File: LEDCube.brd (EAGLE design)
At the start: 100.5 x 80.2 mm, 19 parts

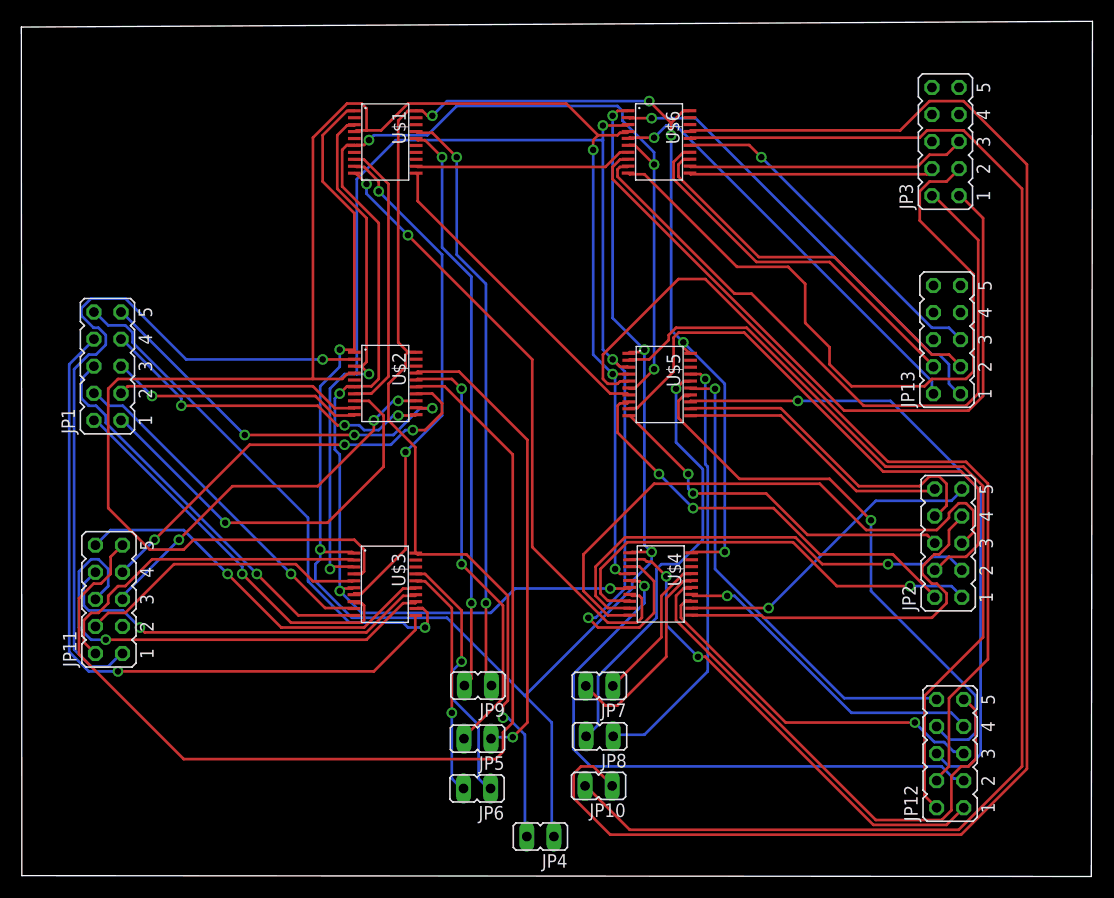
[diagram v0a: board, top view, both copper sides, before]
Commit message: Laid out MSP430 board. Not routed yet.
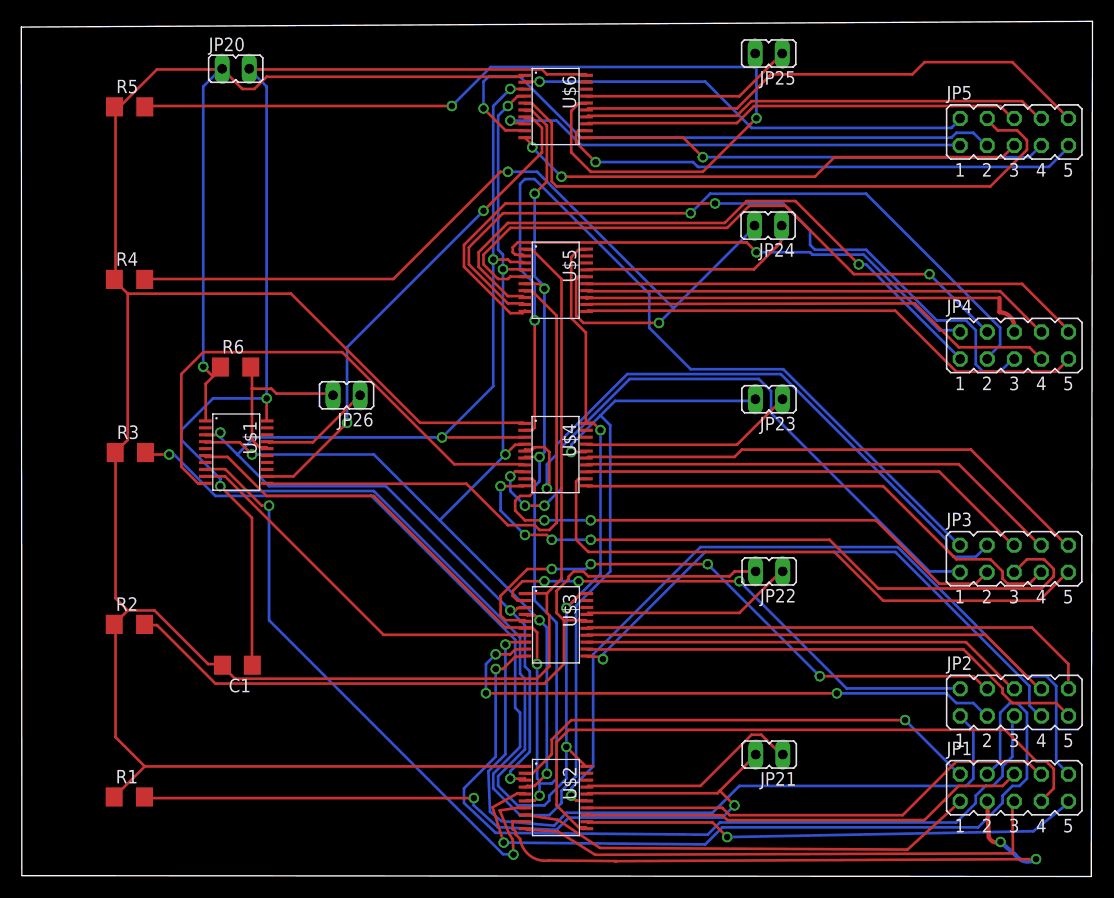
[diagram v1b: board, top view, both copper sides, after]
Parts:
- removed JP10, JP6, JP7, JP8, JP9: (no value), jumper:JP1
- removed JP11, JP12, JP13: (no value), jumper:JP5Q
- added C1: (no value), eagle-ltspice:C1206
- added JP20, JP21, JP22, JP23, JP24, JP25, JP26: (no value), jumper:JP1
- added R1, R2, R3, R4, R5, R6: (no value), rcl:R1206
- JP4, JP5: device jumper:JP1 -> jumper:JP5Q
- moved JP1 93.8 mm to (93.0, 8.52), turned to 0 degrees
- moved JP5 76.0 mm to (93.0, 70.0), turned to 0 degrees
- moved JP4 64.0 mm to (93.0, 50.0), turned to 0 degrees
- moved U$2 42.0 mm to (50.0, 7.60)
- moved JP3 39.7 mm to (93.0, 30.0), turned to 0 degrees
- moved U$1 32.3 mm to (20.0, 40.0)
- moved U$3 16.5 mm to (50.0, 23.8)
- moved JP2 16.2 mm to (93.0, 16.5), turned to 0 degrees
- moved U$4 15.6 mm to (50.0, 39.8)
- moved U$5 13.8 mm to (50.0, 56.1)
- moved U$6 10.3 mm to (50.0, 72.4)
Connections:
- net 0C0: now also JP1.2; no longer JP11.1
- net 0C1: now also JP1.4; no longer JP11.3
- net 0C2: now also JP1.6; no longer JP11.5
- net 0C3: now also JP1.8; no longer JP11.7
- net 0C4: now also JP1.10; no longer JP11.9
- net 1A0: now also JP2.1; no longer JP1.2
- net 1A1: now also JP2.3; no longer JP1.4
- net 1A2: now also JP2.5; no longer JP1.6
- net 1A3: now also JP2.7; no longer JP1.8
- net 1A4: now also JP2.9; no longer JP1.10
- net 1C0: now also JP2.2; no longer JP11.2
- net 1C1: now also JP2.4; no longer JP11.4
- net 1C2: now also JP2.6; no longer JP11.6
- net 1C3: now also JP2.8; no longer JP11.8
- net 1C4: now also JP2.10; no longer JP11.10
- net 2A0: now also JP3.1; no longer JP2.1
- net 2A1: now also JP3.3; no longer JP2.3
- net 2A2: now also JP3.5; no longer JP2.5
- net 2A3: now also JP3.7; no longer JP2.7
- net 2A4: now also JP3.9; no longer JP2.9
- net 2C0: now also JP3.2; no longer JP12.1
- net 2C1: now also JP3.4; no longer JP12.3
- net 2C2: now also JP3.6; no longer JP12.5
- net 2C3: now also JP3.8; no longer JP12.7
- net 2C4: now also JP3.10; no longer JP12.9
- net 3A0: now also JP4.1; no longer JP2.2
- net 3A1: now also JP4.3; no longer JP2.4
- net 3A2: now also JP4.5; no longer JP2.6
- net 3A3: now also JP4.7; no longer JP2.8
- net 3A4: now also JP4.9; no longer JP2.10
- net 3C0: now also JP4.2; no longer JP12.2
- net 3C1: now also JP4.4; no longer JP12.4
- net 3C2: now also JP4.6; no longer JP12.6
- net 3C3: now also JP4.8; no longer JP12.8
- net 3C4: now also JP4.10; no longer JP12.10
- net 4A0: now also JP5.1; no longer JP3.1
- net 4A1: now also JP5.3; no longer JP3.2
- net 4A2: now also JP5.5; no longer JP3.3
- net 4A3: now also JP5.7; no longer JP3.4
- net 4A4: now also JP5.9; no longer JP3.5
- net 4C0: now also JP5.2; no longer JP13.1
- net 4C1: now also JP5.4; no longer JP13.2
- net 4C2: now also JP5.6; no longer JP13.3
- net 4C3: now also JP5.8; no longer JP13.4
- net 4C4: now also JP5.10; no longer JP13.5
- net GND: now also C1.1, JP20.2; no longer JP4.2
- net RST0: now also JP21.2, R1.2; no longer JP5.2
- net RST1: now also JP22.2, R2.2; no longer JP6.2
- net RST2: now also JP23.2, R3.2; no longer JP7.2
- net RST3: now also JP24.2, R4.2; no longer JP8.2
- net RST4: now also JP25.2, R5.2; no longer JP10.2
- net RSTM: now also JP26.2, R6.2; no longer JP9.2
- net TST0: now also JP21.1; no longer JP5.1
- net TST1: now also JP22.1; no longer JP6.1
- net TST2: now also JP23.1; no longer JP7.1
- net TST3: now also JP24.1; no longer JP8.1
- net TST4: now also JP25.1; no longer JP10.1
- net TSTM: now also JP26.1; no longer JP9.1
- net VCC: now also C1.2, JP20.1, R1.1, R2.1, R3.1, R4.1, R5.1, R6.1; no longer JP4.1
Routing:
- net VCC: track 157.4 -> 311.6 mm, vias 5 -> 1
- net TST4: track 145.4 -> 20.0 mm
- net RST2: track 18.8 -> 124.9 mm, vias 0 -> 2
- net 0C1: track 0.00 -> 74.7 mm, vias 0 -> 1
- net SIMO: track 168.6 -> 105.5 mm, vias 3 -> 6
- net GND: track 154.4 -> 216.1 mm, vias 6 -> 5
- net RST1: track 21.9 -> 71.7 mm, vias 1 -> 0
- net TSTM: track 55.7 -> 10.6 mm, vias 2 -> 0
- net RST3: track 40.8 -> 84.5 mm, vias 1 -> 2
- net RST4: track 133.1 -> 92.1 mm, vias 0 -> 2
- net 1A2: track 37.9 -> 77.5 mm
- net 3A2: track 34.5 -> 72.7 mm, vias 2 -> 1
- net RSTM: track 54.1 -> 16.6 mm, vias 2 -> 0
- net 0A1: track 23.1 -> 60.6 mm, vias 0 -> 2
- net 2C0: track 45.0 -> 82.0 mm, vias 2 -> 1
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
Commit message: "LED cube MSP430 PCB that passes DRC and ERC"
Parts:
- moved JP1 60.7 mm to (32.8, 16.1)
- moved JP4 60.0 mm to (33.0, 52.0)
- moved JP5 27.0 mm to (72.8, 52.1)
- moved JP3 20.2 mm to (73.0, 33.1)
- moved JP2 20.0 mm to (73.0, 16.0)
- moved JP26 11.8 mm to (34.4, 34.2)
- moved JP22 4.23 mm to (70.0, 24.6)
- moved JP21 3.98 mm to (70.0, 7.65)
- moved JP24 3.28 mm to (70.4, 64.5)
- moved JP20 2.42 mm to (22.4, 76.3)
- moved JP23 2.37 mm to (70.2, 42.6)
- moved C1 2.09 mm to (18.0, 19.9)
- moved R2 0.21 mm to (9.99, 24.1)
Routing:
- net VCC: track 311.6 -> 228.9 mm, vias 1 -> 3
- net 0C4: track 77.5 -> 21.7 mm, vias 1 -> 2
- net 2C0: track 82.0 -> 26.8 mm, vias 1 -> 2
- net 3A2: track 72.7 -> 18.0 mm, vias 1 -> 0
- net 0C1: track 74.7 -> 24.2 mm
- net 3A1: track 68.9 -> 19.8 mm
- net 1A2: track 77.5 -> 30.5 mm, vias 1 -> 0
- net RST2: track 124.9 -> 84.9 mm, vias 2 -> 1
- net SIMO: track 105.5 -> 143.8 mm
- net 2A2: track 65.2 -> 30.0 mm, vias 4 -> 1
- net 0A1: track 60.6 -> 25.6 mm, vias 2 -> 1
- net 3A0: track 60.2 -> 26.7 mm, vias 1 -> 2
- net 3C1: track 59.5 -> 26.4 mm, vias 1 -> 2
- net 0A3: track 61.8 -> 29.3 mm, vias 0 -> 1
- net 3A4: track 48.1 -> 15.8 mm
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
